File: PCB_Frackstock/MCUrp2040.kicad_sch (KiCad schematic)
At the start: 32 parts, among them J10 SWD, J6 Conn_01x02_Male, J8 Conn_01x02_Male, U1 RP2040, U2 W25Q128JVSIQ, Y1 TAXM12M4RLBDDT2T

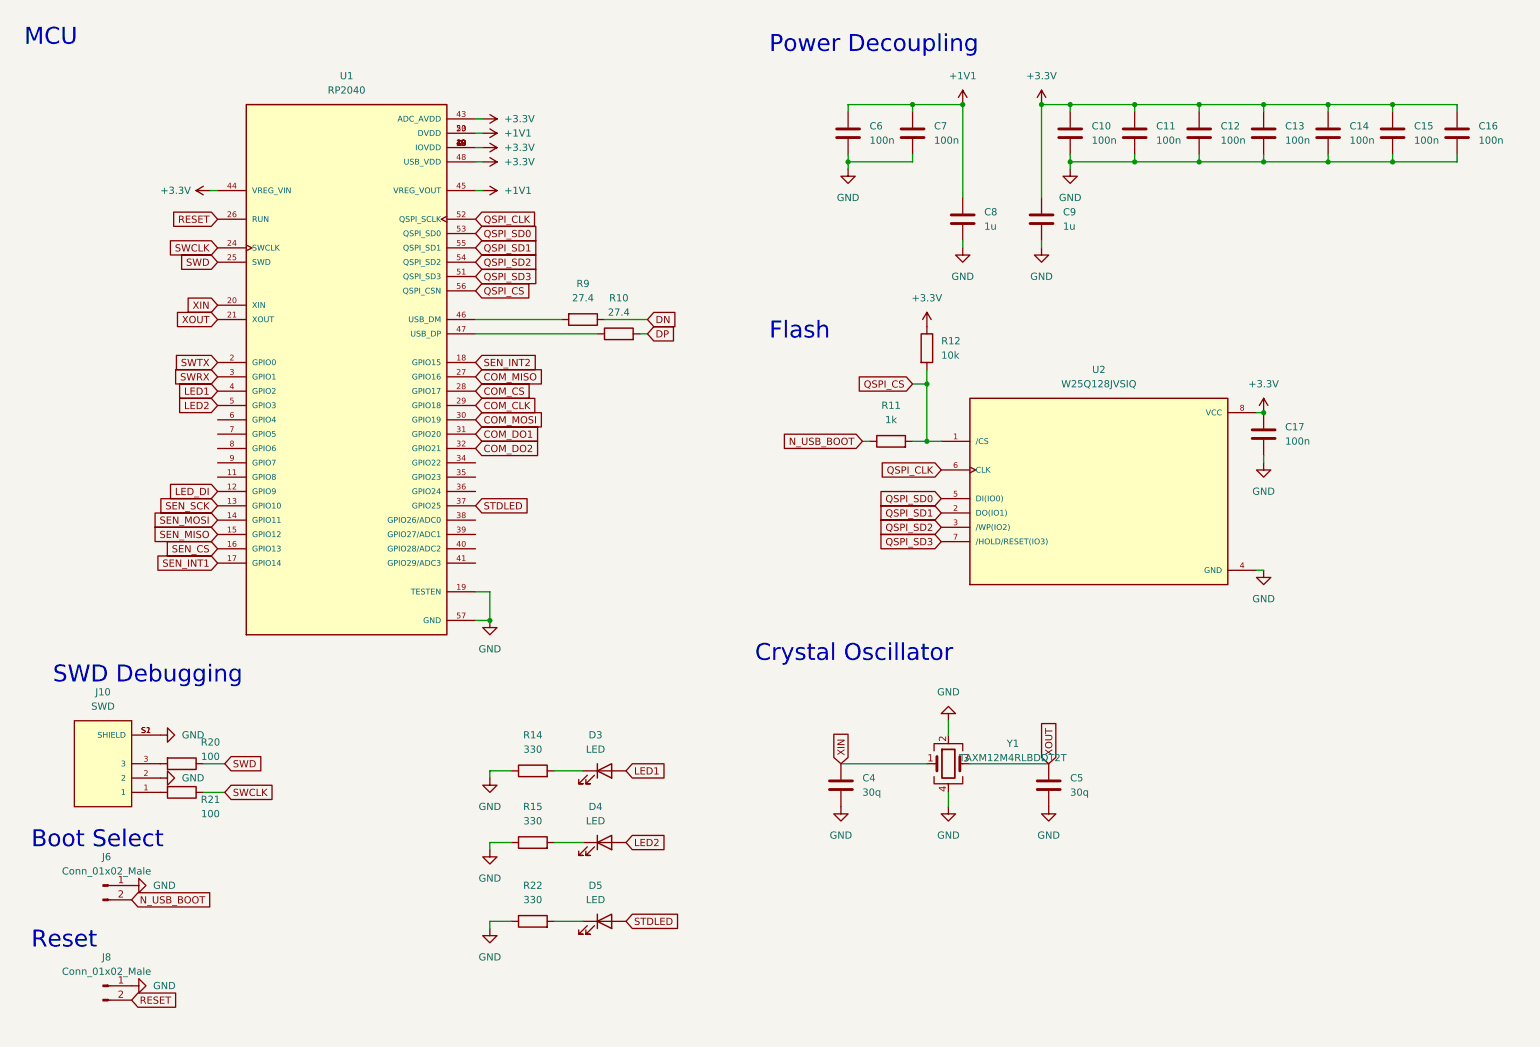
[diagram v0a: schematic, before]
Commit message: Battery Management and change parts to 0603
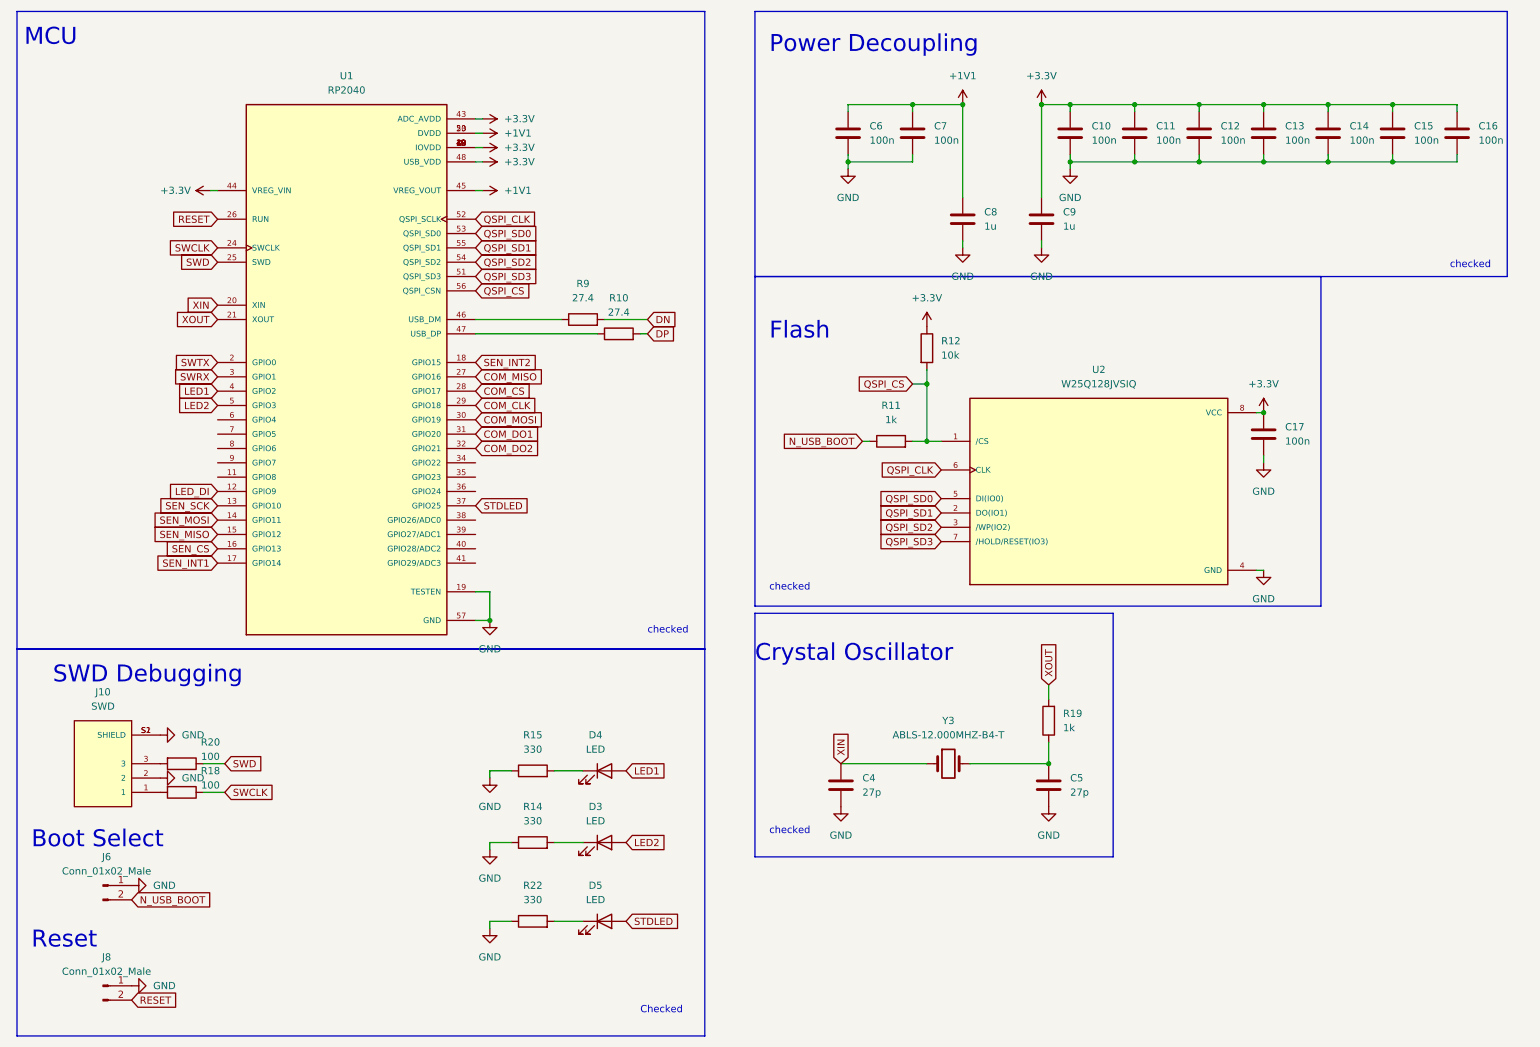
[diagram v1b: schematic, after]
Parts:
- removed R21: 100, Resistor_SMD:R_0201_0603Metric, symbol Device:R
- removed Y1: TAXM12M4RLBDDT2T, Crystal:Crystal_SMD_3225-4Pin_3.2x2.5mm, symbol Device:Crystal_GND24
- added R18: 100, Resistor_SMD:R_0603_1608Metric_Pad0.98x0.95mm_HandSolder, symbol Device:R
- added R19: 1k, Resistor_SMD:R_0603_1608Metric_Pad0.98x0.95mm_HandSolder, symbol Device:R
- added Y3: ABLS-12.000MHZ-B4-T, symbol Device:Crystal
- C10, C11, C12, C13, C14, C15, C16, C17, C6, C7: footprint Capacitor_SMD:C_0201_0603Metric -> Capacitor_SMD:C_0603_1608Metric_Pad1.08x0.95mm_HandSolder; LCSC C66938 -> (none); Note https://www.lcsc.com/product-detail/Multilayer-Ceramic-Capa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 -> (none); Vendor C30926 -> (none); vendor C30926 -> (none)
- C4, C5: value 30q -> 27p; footprint Capacitor_SMD:C_0201_0603Metric -> Capacitor_SMD:C_0603_1608Metric_Pad1.08x0.95mm_HandSolder; LCSC C312064 -> (none); Note https://www.lcsc.com/product-detail/Multilayer-Ceramic-Capa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 -> (none); Vendor C113797 -> (none); vendor C113797 -> (none)
- C8, C9: footprint Capacitor_SMD:C_0201_0603Metric -> Capacitor_SMD:C_0603_1608Metric_Pad1.08x0.95mm_HandSolder; LCSC C87143 -> (none); Note https://www.lcsc.com/product-detail/Multilayer-Ceramic-Capa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 -> (none); Vendor C59302 -> (none); vendor C59302 -> (none)
- D3, D4, D5: footprint LED_SMD:LED_0402_1005Metric -> LED_SMD:LED_0603_1608Metric_Pad1.05x0.95mm_HandSolder; LCSC C434447 -> (none); Note https://www.lcsc.com/product-detail/Light-Emitting-Diodes-L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 -> (none); Vendor C84266 -> (none); vendor C84266 -> (none)
- R10, R9: footprint Resistor_SMD:R_0201_0603Metric -> Resistor_SMD:R_0603_1608Metric_Pad0.98x0.95mm_HandSolder; LCSC C423620 -> (none); Note https://www.lcsc.com/product-detail/Chip-Resistor-Surface-M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 -> (none); Vendor C2907018 -> (none); vendor C2907018 -> (none)
- R11: footprint Resistor_SMD:R_0201_0603Metric -> Resistor_SMD:R_0603_1608Metric_Pad0.98x0.95mm_HandSolder; LCSC C138165 -> (none); Note https://www.lcsc.com/product-detail/Chip-Resistor-Surface-M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 -> (none); Vendor C21190 -> (none); vendor C21190 -> (none)
- R12: footprint Resistor_SMD:R_0201_0603Metric -> Resistor_SMD:R_0603_1608Metric_Pad0.98x0.95mm_HandSolder; LCSC C106225 -> (none); Note https://www.lcsc.com/product-detail/Chip-Resistor-Surface-M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 -> (none); Vendor C25804 -> (none); vendor C25804 -> (none)
- R14, R15, R22: footprint Resistor_SMD:R_0201_0603Metric -> Resistor_SMD:R_0603_1608Metric_Pad0.98x0.95mm_HandSolder; LCSC C851717 -> (none); Note https://www.lcsc.com/product-detail/Chip-Resistor-Surface-M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 -> (none); Vendor C105881 -> (none); vendor C105881 -> (none)
- R20: footprint Resistor_SMD:R_0201_0603Metric -> Resistor_SMD:R_0603_1608Metric_Pad0.98x0.95mm_HandSolder; LCSC C77623 -> (none); Note https://www.lcsc.com/product-detail/Chip-Resistor-Surface-M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 -> (none); Vendor C105588 -> (none); vendor C105588 -> (none)
- U2: LCSC C113767 -> (none); MANUFACTURER Winbond Electronics -> (none); MAXIMUM_PACKAGE_HEIGHT 2.16 mm -> (none); Note https://www.lcsc.com/product-detail/NOR-FLASH_Winbond-Elec-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 -> (none); PARTREV I -> (none); STANDARD IPC-7351B -> (none); Vendor C113767 -> (none); vendor C113767 -> (none)
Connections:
- net DN: now also R9.2; no longer R9.1
- net LED1: now also D4.2 (A); no longer D3.2 (A)
- net LED2: now also D3.2 (A); no longer D4.2 (A)
- net SWCLK: now also R18.1
- net XIN: now also Y3.1
- net XOUT: now also R19.2; no longer C5.1
- net at J10.1: now also R18.2
- net at U1.46 (USB_DM): now also R9.1; no longer R9.2
- new net: C5.1, R19.1, Y3.2
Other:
- note added: "Checked"
- note added: "checked"

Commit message: Schema fertig
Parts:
- removed R19: 1k, Resistor_SMD:R_0603_1608Metric_Pad0.98x0.95mm_HandSolder, symbol Device:R
- C4, C5: value 27p -> 14p
- Y3: value ABLS-12.000MHZ-B4-T -> 12MHz; footprint (none) -> Crystal:Crystal_SMD_5032-2Pin_5.0x3.2mm; Notes (none) -> 445C35A12M00000
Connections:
- net XOUT: now also C5.1, Y3.2

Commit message: Schema_fertig
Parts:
- removed C10, C11, C12, C13, C14, C15, C16, C17, C6, C7: 100n, Capacitor_SMD:C_0603_1608Metric_Pad1.08x0.95mm_HandSolder, symbol Device:C
- removed C4, C5: 14p, Capacitor_SMD:C_0603_1608Metric_Pad1.08x0.95mm_HandSolder, symbol Device:C
- removed C8, C9: 1u, Capacitor_SMD:C_0603_1608Metric_Pad1.08x0.95mm_HandSolder, symbol Device:C
- removed D3, D4, D5: LED, LED_SMD:LED_0603_1608Metric_Pad1.05x0.95mm_HandSolder, symbol Device:LED
- removed J10: SWD, SnapEDA Library:JST_SM03B-SRSS-TB(LF)(SN), symbol SM03B-SRSS-TB_LF__SN_:SM03B-SRSS-TB(LF)(SN)
- removed J6, J8: Conn_01x02_Male, Connector_PinHeader_2.54mm:PinHeader_1x02_P2.54mm_Vertical, symbol Connector:Conn_01x02_Male
- removed R10, R9: 27.4, Resistor_SMD:R_0603_1608Metric_Pad0.98x0.95mm_HandSolder, symbol Device:R
- removed R11: 1k, Resistor_SMD:R_0603_1608Metric_Pad0.98x0.95mm_HandSolder, symbol Device:R
- removed R12: 10k, Resistor_SMD:R_0603_1608Metric_Pad0.98x0.95mm_HandSolder, symbol Device:R
- removed R14, R15, R22: 330, Resistor_SMD:R_0603_1608Metric_Pad0.98x0.95mm_HandSolder, symbol Device:R
- removed R18, R20: 100, Resistor_SMD:R_0603_1608Metric_Pad0.98x0.95mm_HandSolder, symbol Device:R
- removed U1: RP2040, SnapEDA Library:QFN40P700X700X90-57N, symbol RP2040:RP2040
- removed U2: W25Q128JVSIQ, SnapEDA Library:SOIC127P790X216-8N, symbol W25Q128JVSIQ:W25Q128JVSIQ
- removed Y3: 12MHz, Crystal:Crystal_SMD_5032-2Pin_5.0x3.2mm, symbol Device:Crystal
- added J3, J8: Conn_01x03_Pin, Connector_PinHeader_2.54mm:PinHeader_1x03_P2.54mm_Vertical, symbol Connector:Conn_01x03_Pin
- added J4: Conn_01x02_Male, Connector_PinHeader_2.54mm:PinHeader_1x02_P2.54mm_Vertical, symbol Connector:Conn_01x02_Male
- added J5: Conn_01x02_Pin, Connector_PinHeader_2.54mm:PinHeader_1x02_P2.54mm_Vertical, symbol Connector:Conn_01x02_Pin
- added J6: Conn_01x06_Pin, Connector_PinHeader_2.54mm:PinHeader_1x06_P2.54mm_Vertical, symbol Connector:Conn_01x06_Pin
- added J7: Conn_01x04_Pin, Connector_PinHeader_2.54mm:PinHeader_1x04_P2.54mm_Vertical, symbol Connector:Conn_01x04_Pin
- added JP1: SolderJumper_2_Open, Jumper:SolderJumper-2_P1.3mm_Open_RoundedPad1.0x1.5mm, symbol Jumper:SolderJumper_2_Open
- added U1: Pico, Frack:RPi_Pico_SMD_ohne_Debug, symbol Frack:Pico_ohne_Debug
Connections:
- net +3.3V: now also J3.3 (Pin_3), U1.36 (3V3)
- net COM_CLK: now also U1.24 (GPIO18)
- net COM_CS: now also U1.22 (GPIO17)
- net COM_DO1: now also U1.26 (GPIO20)
- net COM_DO2: now also U1.27 (GPIO21)
- net COM_MISO: now also U1.21 (GPIO16)
- net COM_MOSI: now also U1.25 (GPIO19)
- net GND: now also J4.1 (Pin_1), J6.1 (Pin_1), J6.2 (Pin_2), J6.3 (Pin_3), J6.4 (Pin_4), J6.5 (Pin_5), J6.6 (Pin_6), U1.13 (GND), U1.18 (GND), U1.23 (GND), U1.28 (GND), U1.3 (GND), U1.33 (AGND), U1.38 (GND), U1.8 (GND)
- net LED_DI: now also U1.12 (GPIO9)
- net RESET: now also J4.2 (Pin_2), U1.30 (RUN)
- net SEN_CS: now also U1.17 (GPIO13)
- net SEN_INT1: now also U1.19 (GPIO14)
- net SEN_INT2: now also U1.20 (GPIO15)
- net SEN_MISO: now also U1.16 (GPIO12)
- net SEN_MOSI: now also U1.15 (GPIO11)
- net SEN_SCK: now also U1.14 (GPIO10)
- new net: JP1.1 (A), U1.40 (VBUS)
- new net BAT_O: J3.1 (Pin_1), J3.2 (Pin_2), U1.39 (VSYS)
- new net GP2: J7.4 (Pin_4), U1.4 (GPIO2)
- new net GP3: J7.3 (Pin_3), U1.5 (GPIO3)
- new net GP4: J7.2 (Pin_2), U1.6 (GPIO4)
- new net GP5: J7.1 (Pin_1), U1.7 (GPIO5)
- new net GP6: J8.3 (Pin_3), U1.9 (GPIO6)
- new net GP7: J8.2 (Pin_2), U1.10 (GPIO7)
- new net GP8: J8.1 (Pin_1), U1.11 (GPIO8)
- new net UART0_RX: J5.1 (Pin_1), U1.2 (GPIO1)
- new net UART0_TX: J5.2 (Pin_2), U1.1 (GPIO0)
- new net VBUS: JP1.2 (B)
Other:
- note removed: "Boot Select"
- note removed: "Checked"
- note removed: "Crystal Oscillator"
- note removed: "Flash"
- note removed: "MCU"
- note removed: "Power Decoupling"
- note removed: "SWD Debugging"
- note removed: "checked"

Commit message: Layout Fertig
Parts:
- removed J3, J8: Conn_01x03_Pin, Connector_PinHeader_2.54mm:PinHeader_1x03_P2.54mm_Vertical, symbol Connector:Conn_01x03_Pin
- removed J4: Conn_01x02_Male, Connector_PinHeader_2.54mm:PinHeader_1x02_P2.54mm_Vertical, symbol Connector:Conn_01x02_Male
- removed J5: Conn_01x02_Pin, Connector_PinHeader_2.54mm:PinHeader_1x02_P2.54mm_Vertical, symbol Connector:Conn_01x02_Pin
- removed J6: Conn_01x06_Pin, Connector_PinHeader_2.54mm:PinHeader_1x06_P2.54mm_Vertical, symbol Connector:Conn_01x06_Pin
- removed J7: Conn_01x04_Pin, Connector_PinHeader_2.54mm:PinHeader_1x04_P2.54mm_Vertical, symbol Connector:Conn_01x04_Pin
- added J3, J4: Conn_01x06_Pin, Frack:PinHeader_2x03_P2.54mm_Vertical_SMD_kleiner, symbol Connector:Conn_01x06_Pin
- added TP1: TestPoint_Alt, TestPoint:TestPoint_Pad_D1.5mm, symbol Connector:TestPoint_Alt
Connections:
- net +3.3V: now also J4.4 (Pin_4)
- net BAT_O: now also J4.5 (Pin_5), J4.6 (Pin_6)
- net GND: now also J4.2 (Pin_2), J4.3 (Pin_3)
- net GP2: now also J3.3 (Pin_3)
- net GP3: now also J3.4 (Pin_4)
- net GP4: now also J3.5 (Pin_5)
- net GP5: now also J3.6 (Pin_6)
- net RESET: now also J4.1 (Pin_1)
- net UART0_RX: now also J3.2 (Pin_2)
- net UART0_TX: now also J3.1 (Pin_1)
- net SDA: now reaches U1.31 (GPIO26_ADC0)
- net SCL: now reaches U1.32 (GPIO27_ADC1)
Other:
- note removed: "Reset"

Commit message: Layout Update
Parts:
- removed TP1: TestPoint_Alt, TestPoint:TestPoint_Pad_D1.5mm, symbol Connector:TestPoint_Alt
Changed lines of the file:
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@@
-    (stroke (width 0) (type default))
-  )
-  (wire (pts (xy 30.48 129.54) (xy 35.56 129.54))
     (stroke (width 0) (type default))
   )
@@
         )
       )
-    )
-  )
-  (symbol (lib_id "Connector:TestPoint_Alt") (at 35.56 129.54 0) (unit 1)
-    (in_bom yes) (on_board yes) (dnp no)
-    (property "Reference" "TP1" (at 35.56 123.19 0)
-      (effects (font (size 1.27 1.27)) (justify left))
-    )
-    (property "Value" "TestPoint_Alt" (at 36.83 130.81 0)
-      (effects (font (size 1.27 1.27)) (justify left) hide)
-    )
-    (property "Footprint" "TestPoint:TestPoint_Pad_D1.5mm" (at 40.64 129.54 0)
-      (effects (font (size 1.27 1.27)) hide)
-    )
-    (property "Datasheet" "~" (at 40.64 129.54 0)
-      (effects (font (size 1.27 1.27)) hide)
-    )
-    (property "Info" "DM" (at 35.56 129.54 0)
-      (effects (font (size 1.27 1.27)) hide)
-    )
-    (pin "1")
-    (instances
-      (project "Frackstock"
-        (path "/d92252e1-c687-49e6-87c8-e9430a2c933e/e9af0e5f-81d9-4941-b623-a8314cc9a540"
-          (reference "TP1") (unit 1)
-        )
-        (path "/d92252e1-c687-49e6-87c8-e9430a2c933e/ef112b53-3ef3-47e6-bd33-16e434e7b229"
-          (reference "RESET1") (unit 1)
-        )
-      )

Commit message: Frackstock-Schema-review1.0
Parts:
- added J2: 105450-0101, SnapEDA Library pretty:MOLEX_105450-0101, symbol 105450-0101:105450-0101
- added R1, R2: 5.1k, Resistor_SMD:R_0603_1608Metric_Pad0.98x0.95mm_HandSolder, symbol Device:R
- added TP1, TP2: TestPoint_Alt, Frack:TestPoint_Pad_1.5x1.5mm_small, symbol Connector:TestPoint_Alt
- added TP3: TestPoint_Alt, TestPoint:TestPoint_Pad_1.5x1.5mm, symbol Connector:TestPoint_Alt
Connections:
- net GND: now also J2.A1 (GND1), J2.A12 (GND2), J2.B1 (GND3), J2.B12 (GND4), J2.S1 (SHIELD), J2.S2 (SHIELD__1), J2.S3 (SHIELD__2), J2.S4 (SHIELD__3), R1.1, R2.1, TP3.1
- net VBUS: now also J2.A4 (VBUS1), J2.A9 (VBUS2), J2.B4 (VBUS3), J2.B9 (VBUS4)
- new net: J2.A5 (CC1), R1.2
- new net: J2.B5 (CC2), R2.2
- new net DN: J2.A7 (D1-), J2.B7 (D2-), TP1.1
- new net DP: J2.A6 (D1+), J2.B6 (D2+), TP2.1
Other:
- note added: "USB-C 5V 3A"
- note added: "checked"

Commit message: Schema-review-1
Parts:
- added C18, C19: 100n, Capacitor_SMD:C_0603_1608Metric_Pad1.08x0.95mm_HandSolder, symbol Device:C
- added C33: 330u, Capacitor_SMD:C_0805_2012Metric_Pad1.18x1.45mm_HandSolder, symbol Device:C
- added J1: Conn_02x03_Pin, Frack:PinHeader_2x03_P2.54mm_Vertical_SMD_kleiner, symbol Connector:Conn_01x06_Pin
- added R16: 470, Resistor_SMD:R_0603_1608Metric_Pad0.98x0.95mm_HandSolder, symbol Device:R
- added R2 (x2): 27, Resistor_SMD:R_0603_1608Metric_Pad0.98x0.95mm_HandSolder, symbol Device:R
- added U7: BMI160, Frack:PQFN50P250X300X88-14N, symbol BMI160:BMI160
- J3, J4: value Conn_01x06_Pin -> Conn_02x03_Pin
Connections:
- net +3.3V: now also C18.1, C19.1, J1.3 (Pin_3), U7.5 (VDDIO), U7.8 (VDD)
- net BAT_O: now also C33.2, J1.4 (Pin_4)
- net DN: now also R2.2; no longer TP1.1
- net DP: now also R2.2; no longer TP2.1
- net GND: now also C18.2, C19.2, C33.1, J1.1 (Pin_1), U7.6 (GNDIO), U7.7 (GND)
- net SEN_CS: now also U7.12 (CSB)
- net SEN_INT1: now also U7.4 (INT1)
- net SEN_INT2: now also U7.9 (INT2)
- net SEN_MISO: now also U7.1 (SDO)
- net SEN_MOSI: now also U7.14 (SDX)
- net SEN_SCK: now also U7.13 (SCX)
- net GP2 renamed GPIO2
- net GP3 renamed GPIO3
- net GP4 renamed GPIO4
- net GP5 renamed GPIO5
- net GP6: no longer names the net of U1.9 (GPIO6)
- net GP7: no longer names the net of U1.10 (GPIO7)
- net GP8: no longer names the net of U1.11 (GPIO8)
- net LED_DI renamed LED_EXT
- net LED_EXT: now also R16.1
- net SCL renamed SCL_EXT
- net SCL_EXT: now also J1.6 (Pin_6)
- net SDA renamed SDA_EXT
- net SDA_EXT: now also J1.5 (Pin_5)
- new net: R2.1, TP2.1
- new net: R2.1, TP1.1
- new net: J1.2 (Pin_2), R16.2
- no-connect marks 0 -> 21
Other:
- note added: "MEMS Acceleration Sensor"
- note added: "Pi Pico"
- note added: "RGB LEDs"
- note added: "USB Pi Pico"
- note removed: "checked"
- company: (none) -> Eberkreis
- title: (none) -> Frackstock ET2024
- moved on the sheet: J2, J3, J4, JP1, R1, R2, TP1, TP2, TP3, U1

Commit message: Fracstock PCB final commit
DRC check, PCB review done, ready to order
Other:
- company: Eberkreis -> Eberkreis Engineering
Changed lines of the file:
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@@
     (date "2024-03-24")
     (rev "2")
-    (company "Eberkreis")
+    (company "Eberkreis Engineering")
   )
   (junction (at 76.2 44.45) (diameter 0) (color 0 0 0 0)
